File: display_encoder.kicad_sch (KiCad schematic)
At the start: 9 parts

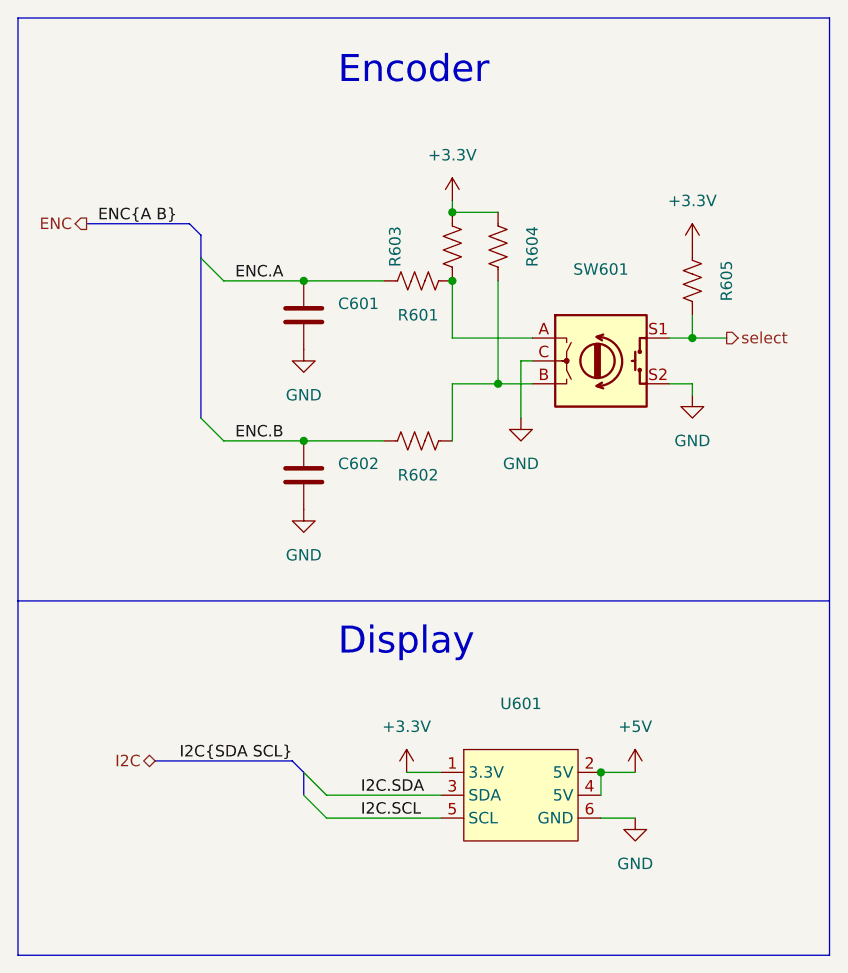
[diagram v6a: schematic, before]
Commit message: Fix and tune differential pair and zones
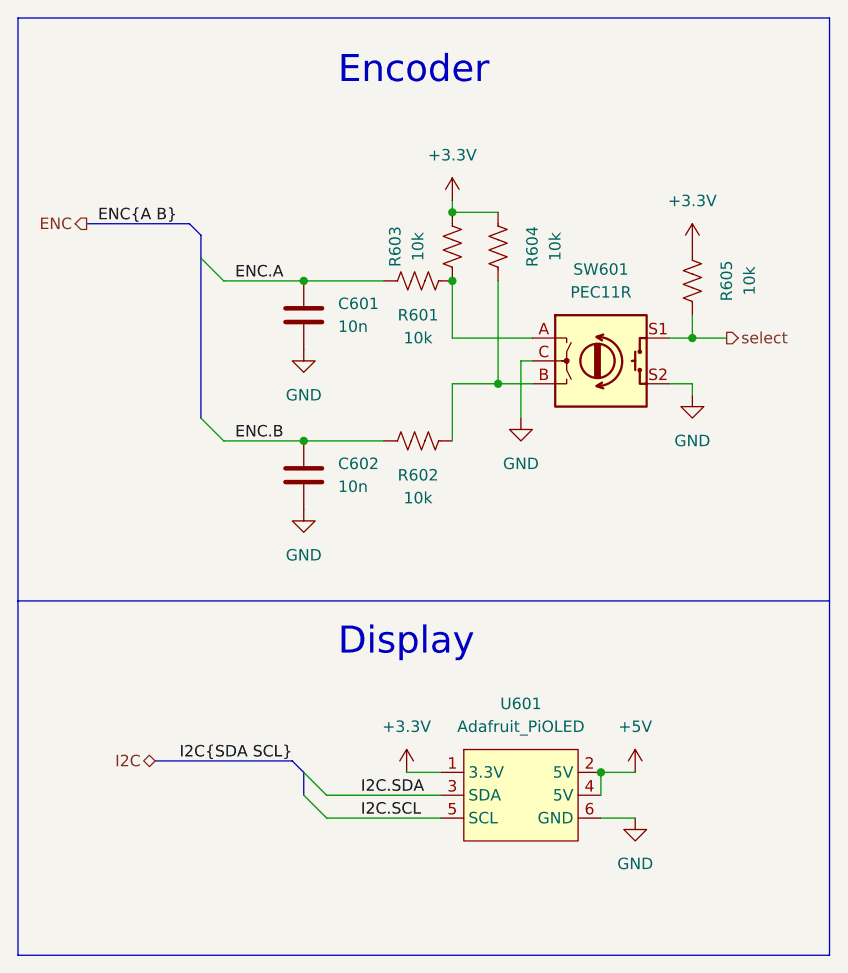
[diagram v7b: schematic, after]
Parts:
- C601, C602: value (none) -> 10n; footprint (none) -> Capacitor_SMD:C_0805_2012Metric
- R601, R602, R603, R604, R605: value (none) -> 10k; footprint (none) -> Resistor_SMD:R_0805_2012Metric
- SW601: value (none) -> PEC11R; footprint (none) -> Rotary_Encoder:RotaryEncoder_Alps_EC12E-Switch_Vertical_H20mm
- U601: value (none) -> Adafruit_PiOLED; footprint (none) -> 0_Display:PiOLED
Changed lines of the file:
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@@
     (in_bom yes) (on_board yes)
     (property "Reference" "R601" (id 0) (at 149.86 73.66 90))
-    (property "Value" "" (id 1) (at 149.86 76.2 90))
-    (property "Footprint" "" (id 2) (at 150.114 68.834 90)
+    (property "Value" "10k" (id 1) (at 149.86 76.2 90))
+    (property "Footprint" "Resistor_SMD:R_0805_2012Metric" (id 2) (at 150.114 68.834 90)
       (effects (font (size 1.27 1.27)) hide)
     )
@@
     (in_bom yes) (on_board yes) (fields_autoplaced)
     (property "Reference" "U601" (id 0) (at 161.29 116.84 0))
-    (property "Value" "" (id 1) (at 161.29 119.38 0))
-    (property "Footprint" "" (id 2) (at 162.56 121.92 0)
+    (property "Value" "Adafruit_PiOLED" (id 1) (at 161.29 119.38 0))
+    (property "Footprint" "0_Display:PiOLED" (id 2) (at 162.56 121.92 0)
       (effects (font (size 1.27 1.27)) hide)
     )
@@
       (effects (font (size 1.27 1.27)) (justify right))
     )
-    (property "Value" "" (id 1) (at 140.97 74.9299 0)
-      (effects (font (size 1.27 1.27)) (justify right))
-    )
-    (property "Footprint" "" (id 2) (at 136.1948 69.85 0)
+    (property "Value" "10n" (id 1) (at 140.97 74.9299 0)
+      (effects (font (size 1.27 1.27)) (justify right))
+    )
+    (property "Footprint" "Capacitor_SMD:C_0805_2012Metric" (id 2) (at 136.1948 69.85 0)
       (effects (font (size 1.27 1.27)) hide)
     )
@@
     (in_bom yes) (on_board yes)
     (property "Reference" "SW601" (id 0) (at 170.18 68.58 0))
-    (property "Value" "" (id 1) (at 170.18 71.12 0))
-    (property "Footprint" "" (id 2) (at 166.37 74.676 0)
+    (property "Value" "PEC11R" (id 1) (at 170.18 71.12 0))
+    (property "Footprint" "Rotary_Encoder:RotaryEncoder_Alps_EC12E-Switch_Vertical_H20mm" (id 2) (at 166.37 74.676 0)
       (effects (font (size 1.27 1.27)) hide)
     )
@@
       (effects (font (size 1.27 1.27)) (justify right))
     )
-    (property "Value" "" (id 1) (at 140.97 92.7099 0)
-      (effects (font (size 1.27 1.27)) (justify right))
-    )
-    (property "Footprint" "" (id 2) (at 136.1948 87.63 0)
+    (property "Value" "10n" (id 1) (at 140.97 92.7099 0)
+      (effects (font (size 1.27 1.27)) (justify right))
+    )
+    (property "Footprint" "Capacitor_SMD:C_0805_2012Metric" (id 2) (at 136.1948 87.63 0)
       (effects (font (size 1.27 1.27)) hide)
     )
@@
     (in_bom yes) (on_board yes)
     (property "Reference" "R603" (id 0) (at 147.32 66.04 90))
-    (property "Value" "" (id 1) (at 149.86 66.04 90))
-    (property "Footprint" "" (id 2) (at 154.686 66.294 90)
+    (property "Value" "10k" (id 1) (at 149.86 66.04 90))
+    (property "Footprint" "Resistor_SMD:R_0805_2012Metric" (id 2) (at 154.686 66.294 90)
       (effects (font (size 1.27 1.27)) hide)
     )
@@
     (in_bom yes) (on_board yes)
     (property "Reference" "R605" (id 0) (at 184.15 69.85 90))
-    (property "Value" "" (id 1) (at 186.69 69.85 90))
-    (property "Footprint" "" (id 2) (at 179.324 69.596 90)
+    (property "Value" "10k" (id 1) (at 186.69 69.85 90))
+    (property "Footprint" "Resistor_SMD:R_0805_2012Metric" (id 2) (at 179.324 69.596 90)
       (effects (font (size 1.27 1.27)) hide)
     )
@@
     (in_bom yes) (on_board yes)
     (property "Reference" "R602" (id 0) (at 149.86 91.44 90))
-    (property "Value" "" (id 1) (at 149.86 93.98 90))
-    (property "Footprint" "" (id 2) (at 150.114 86.614 90)
+    (property "Value" "10k" (id 1) (at 149.86 93.98 90))
+    (property "Footprint" "Resistor_SMD:R_0805_2012Metric" (id 2) (at 150.114 86.614 90)
       (effects (font (size 1.27 1.27)) hide)
     )
@@
     (in_bom yes) (on_board yes)
     (property "Reference" "R604" (id 0) (at 162.56 66.04 90))
-    (property "Value" "" (id 1) (at 165.1 66.04 90))
-    (property "Footprint" "" (id 2) (at 157.734 65.786 90)
-      (effects (font (size 1.27 1.27)) hide)
-    )
+    (property "Value" "10k" (id 1) (at 165.1 66.04 90))
+    (property "Footprint" "Resistor_SMD:R_0805_2012Metric" (id 2) (at 157.734 65.786 90)
+      (effects (font (size 1.27 1.27)) hide)
+    )

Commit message: Add partnumbers
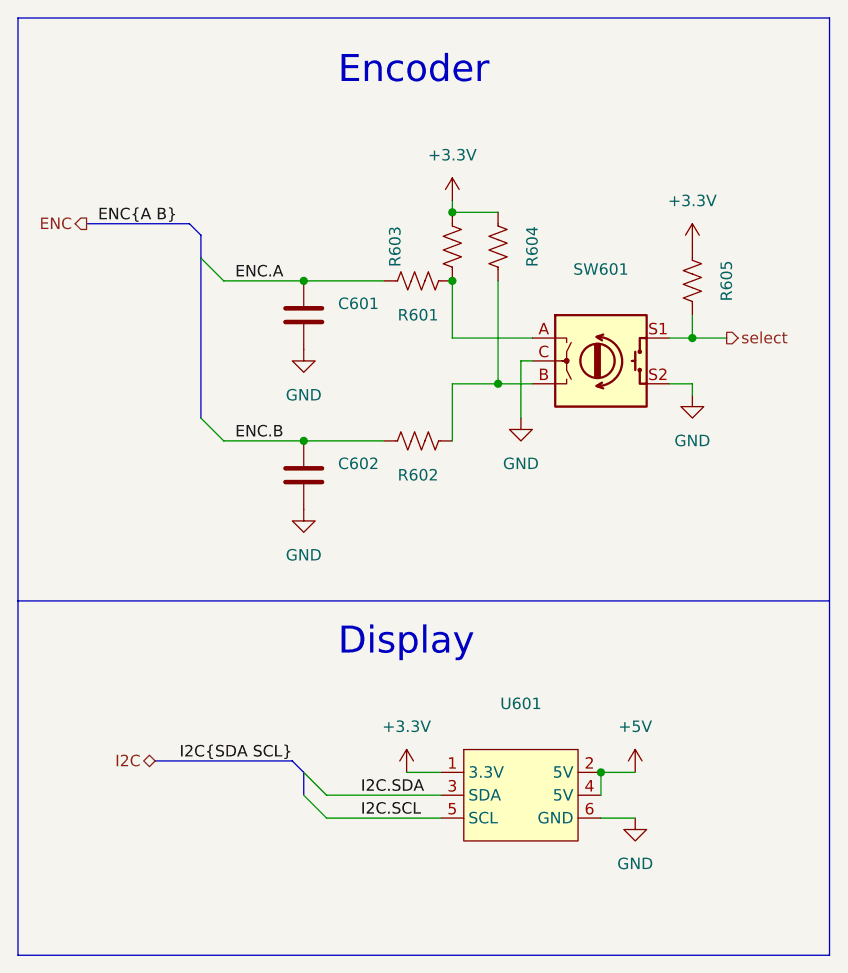
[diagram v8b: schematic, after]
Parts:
- C601, C602: value 10n -> (none); footprint Capacitor_SMD:C_0805_2012Metric -> (none); Manufacturer (none) -> Generic; PartNumber (none) -> Generic
- R601, R602, R603, R604, R605: value 10k -> (none); footprint Resistor_SMD:R_0805_2012Metric -> (none); Manufacturer (none) -> Generic; PartNumber (none) -> Generic
- SW601: value PEC11R -> (none); footprint Rotary_Encoder:RotaryEncoder_Alps_EC12E-Switch_Vertical_H20mm -> (none)
- U601: value Adafruit_PiOLED -> (none); footprint 0_Display:PiOLED -> (none); PartNumber (none) -> PiOled
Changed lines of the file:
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@@
     (in_bom yes) (on_board yes)
     (property "Reference" "R601" (id 0) (at 149.86 73.66 90))
-    (property "Value" "10k" (id 1) (at 149.86 76.2 90))
-    (property "Footprint" "Resistor_SMD:R_0805_2012Metric" (id 2) (at 150.114 68.834 90)
+    (property "Value" "" (id 1) (at 149.86 76.2 90))
+    (property "Footprint" "" (id 2) (at 150.114 68.834 90)
       (effects (font (size 1.27 1.27)) hide)
     )
@@
       (effects (font (size 1.27 1.27)) hide)
     )
+    (property "Manufacturer" "Generic" (id 4) (at 149.86 69.85 0)
+      (effects (font (size 1.27 1.27)) hide)
+    )
+    (property "PartNumber" "Generic" (id 5) (at 149.86 69.85 0)
+      (effects (font (size 1.27 1.27)) hide)
+    )
     (pin "1")
     (pin "2")
@@
     (in_bom yes) (on_board yes) (fields_autoplaced)
     (property "Reference" "U601" (id 0) (at 161.29 116.84 0))
-    (property "Value" "Adafruit_PiOLED" (id 1) (at 161.29 119.38 0))
-    (property "Footprint" "0_Display:PiOLED" (id 2) (at 162.56 121.92 0)
+    (property "Value" "" (id 1) (at 161.29 119.38 0))
+    (property "Footprint" "" (id 2) (at 162.56 121.92 0)
       (effects (font (size 1.27 1.27)) hide)
     )
@@
     )
     (property "Manufacturer" "Adafruit" (id 4) (at 161.29 127 0)
+      (effects (font (size 1.27 1.27)) hide)
+    )
+    (property "PartNumber" "PiOled" (id 5) (at 161.29 127 0)
       (effects (font (size 1.27 1.27)) hide)
     )
@@
       (effects (font (size 1.27 1.27)) (justify right))
     )
-    (property "Value" "10n" (id 1) (at 140.97 74.9299 0)
-      (effects (font (size 1.27 1.27)) (justify right))
-    )
-    (property "Footprint" "Capacitor_SMD:C_0805_2012Metric" (id 2) (at 136.1948 69.85 0)
+    (property "Value" "" (id 1) (at 140.97 74.9299 0)
+      (effects (font (size 1.27 1.27)) (justify right))
+    )
+    (property "Footprint" "" (id 2) (at 136.1948 69.85 0)
       (effects (font (size 1.27 1.27)) hide)
     )
@@
       (effects (font (size 1.27 1.27)) hide)
     )
+    (property "Manufacturer" "Generic" (id 4) (at 137.16 73.66 0)
+      (effects (font (size 1.27 1.27)) hide)
+    )
+    (property "PartNumber" "Generic" (id 5) (at 137.16 73.66 0)
+      (effects (font (size 1.27 1.27)) hide)
+    )
     (pin "1")
     (pin "2")
@@
     (in_bom yes) (on_board yes)
     (property "Reference" "SW601" (id 0) (at 170.18 68.58 0))
-    (property "Value" "PEC11R" (id 1) (at 170.18 71.12 0))
-    (property "Footprint" "Rotary_Encoder:RotaryEncoder_Alps_EC12E-Switch_Vertical_H20mm" (id 2) (at 166.37 74.676 0)
+    (property "Value" "" (id 1) (at 170.18 71.12 0))
+    (property "Footprint" "" (id 2) (at 166.37 74.676 0)
       (effects (font (size 1.27 1.27)) hide)
     )
@@
       (effects (font (size 1.27 1.27)) (justify right))
     )
-    (property "Value" "10n" (id 1) (at 140.97 92.7099 0)
-      (effects (font (size 1.27 1.27)) (justify right))
-    )
-    (property "Footprint" "Capacitor_SMD:C_0805_2012Metric" (id 2) (at 136.1948 87.63 0)
+    (property "Value" "" (id 1) (at 140.97 92.7099 0)
+      (effects (font (size 1.27 1.27)) (justify right))
+    )
+    (property "Footprint" "" (id 2) (at 136.1948 87.63 0)
       (effects (font (size 1.27 1.27)) hide)
     )
     (property "Datasheet" "~" (id 3) (at 137.16 91.44 0)
+      (effects (font (size 1.27 1.27)) hide)
+    )
+    (property "Manufacturer" "Generic" (id 4) (at 137.16 91.44 0)
+      (effects (font (size 1.27 1.27)) hide)
+    )
+    (property "PartNumber" "Generic" (id 5) (at 137.16 91.44 0)
       (effects (font (size 1.27 1.27)) hide)
     )
@@
     (in_bom yes) (on_board yes)
     (property "Reference" "R603" (id 0) (at 147.32 66.04 90))
-    (property "Value" "10k" (id 1) (at 149.86 66.04 90))
-    (property "Footprint" "Resistor_SMD:R_0805_2012Metric" (id 2) (at 154.686 66.294 90)
+    (property "Value" "" (id 1) (at 149.86 66.04 90))
+    (property "Footprint" "" (id 2) (at 154.686 66.294 90)
       (effects (font (size 1.27 1.27)) hide)
     )
@@
       (effects (font (size 1.27 1.27)) hide)
     )
+    (property "Manufacturer" "Generic" (id 4) (at 153.67 66.04 0)
+      (effects (font (size 1.27 1.27)) hide)
+    )
+    (property "PartNumber" "Generic" (id 5) (at 153.67 66.04 0)
+      (effects (font (size 1.27 1.27)) hide)
+    )
     (pin "1")
     (pin "2")
@@
     (in_bom yes) (on_board yes)
     (property "Reference" "R605" (id 0) (at 184.15 69.85 90))
-    (property "Value" "10k" (id 1) (at 186.69 69.85 90))
-    (property "Footprint" "Resistor_SMD:R_0805_2012Metric" (id 2) (at 179.324 69.596 90)
+    (property "Value" "" (id 1) (at 186.69 69.85 90))
+    (property "Footprint" "" (id 2) (at 179.324 69.596 90)
       (effects (font (size 1.27 1.27)) hide)
     )
     (property "Datasheet" "~" (id 3) (at 180.34 69.85 0)
+      (effects (font (size 1.27 1.27)) hide)
+    )
+    (property "Manufacturer" "Generic" (id 4) (at 180.34 69.85 0)
+      (effects (font (size 1.27 1.27)) hide)
+    )
+    (property "PartNumber" "Generic" (id 5) (at 180.34 69.85 0)
       (effects (font (size 1.27 1.27)) hide)
     )
@@
     (in_bom yes) (on_board yes)
     (property "Reference" "R602" (id 0) (at 149.86 91.44 90))
-    (property "Value" "10k" (id 1) (at 149.86 93.98 90))
-    (property "Footprint" "Resistor_SMD:R_0805_2012Metric" (id 2) (at 150.114 86.614 90)
+    (property "Value" "" (id 1) (at 149.86 93.98 90))
+    (property "Footprint" "" (id 2) (at 150.114 86.614 90)
       (effects (font (size 1.27 1.27)) hide)
     )
     (property "Datasheet" "~" (id 3) (at 149.86 87.63 0)
+      (effects (font (size 1.27 1.27)) hide)
+    )
+    (property "Manufacturer" "Generic" (id 4) (at 149.86 87.63 0)
+      (effects (font (size 1.27 1.27)) hide)
+    )
+    (property "PartNumber" "Generic" (id 5) (at 149.86 87.63 0)
       (effects (font (size 1.27 1.27)) hide)
     )
@@
     (in_bom yes) (on_board yes)
     (property "Reference" "R604" (id 0) (at 162.56 66.04 90))
-    (property "Value" "10k" (id 1) (at 165.1 66.04 90))
-    (property "Footprint" "Resistor_SMD:R_0805_2012Metric" (id 2) (at 157.734 65.786 90)
+    (property "Value" "" (id 1) (at 165.1 66.04 90))
+    (property "Footprint" "" (id 2) (at 157.734 65.786 90)
       (effects (font (size 1.27 1.27)) hide)
     )
@@
       (effects (font (size 1.27 1.27)) hide)
     )
+    (property "Manufacturer" "Generic" (id 4) (at 158.75 66.04 0)
+      (effects (font (size 1.27 1.27)) hide)
+    )
+    (property "PartNumber" "Generic" (id 5) (at 158.75 66.04 0)
+      (effects (font (size 1.27 1.27)) hide)
+    )
